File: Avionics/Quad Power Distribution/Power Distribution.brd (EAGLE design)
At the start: 50 x 50 mm, 55 parts, among them U1 LMP8645, U10 SERVOPLUGTHROUGHHOLE_0.1PITCH, U2 LMP8645, U3 LMP8645, U4 LMP8645, U5 LMP8645, U6 ADP2302, U7 SERVOPLUGTHROUGHHOLE_0.1PITCH, U8 SERVOPLUGTHROUGHHOLE_0.1PITCH, U9 SERVOPLUGTHROUGHHOLE_0.1PITCH

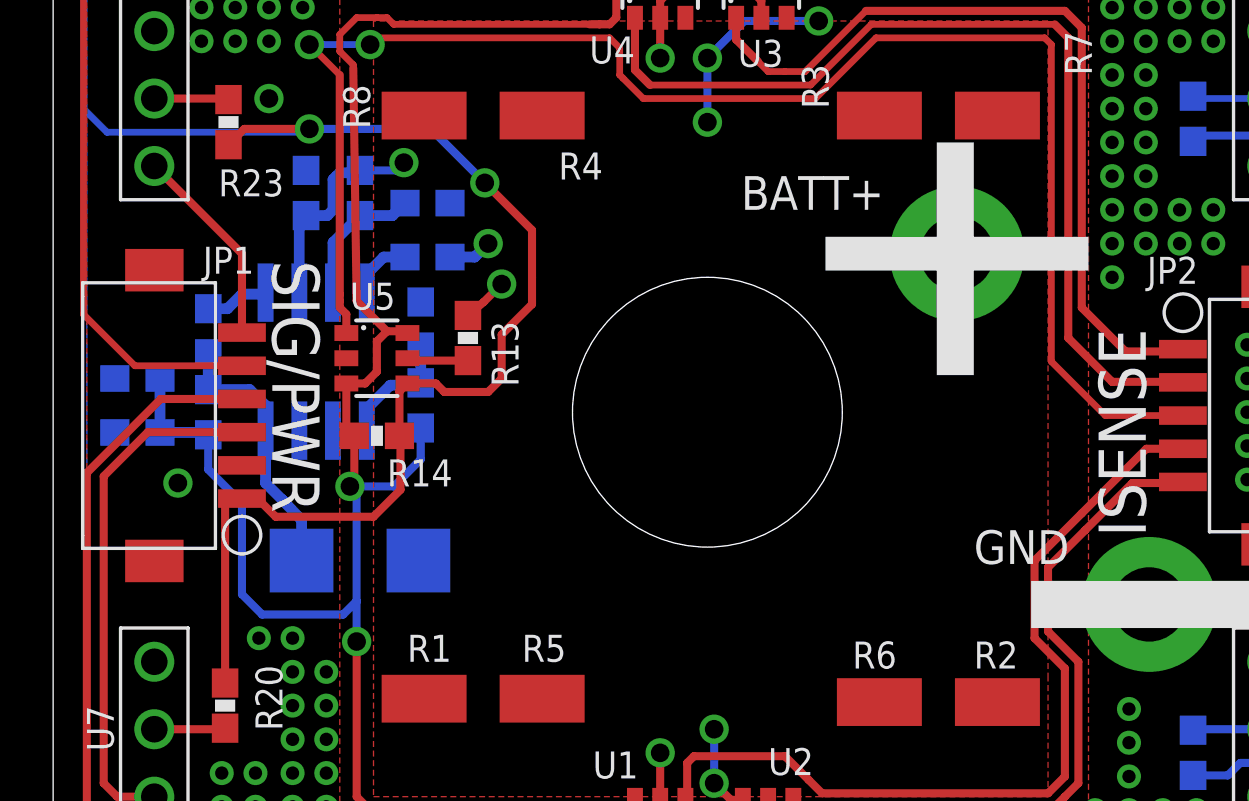
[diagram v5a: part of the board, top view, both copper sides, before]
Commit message: Committed file outputs and cleaned silk. Added shock hazard symbol
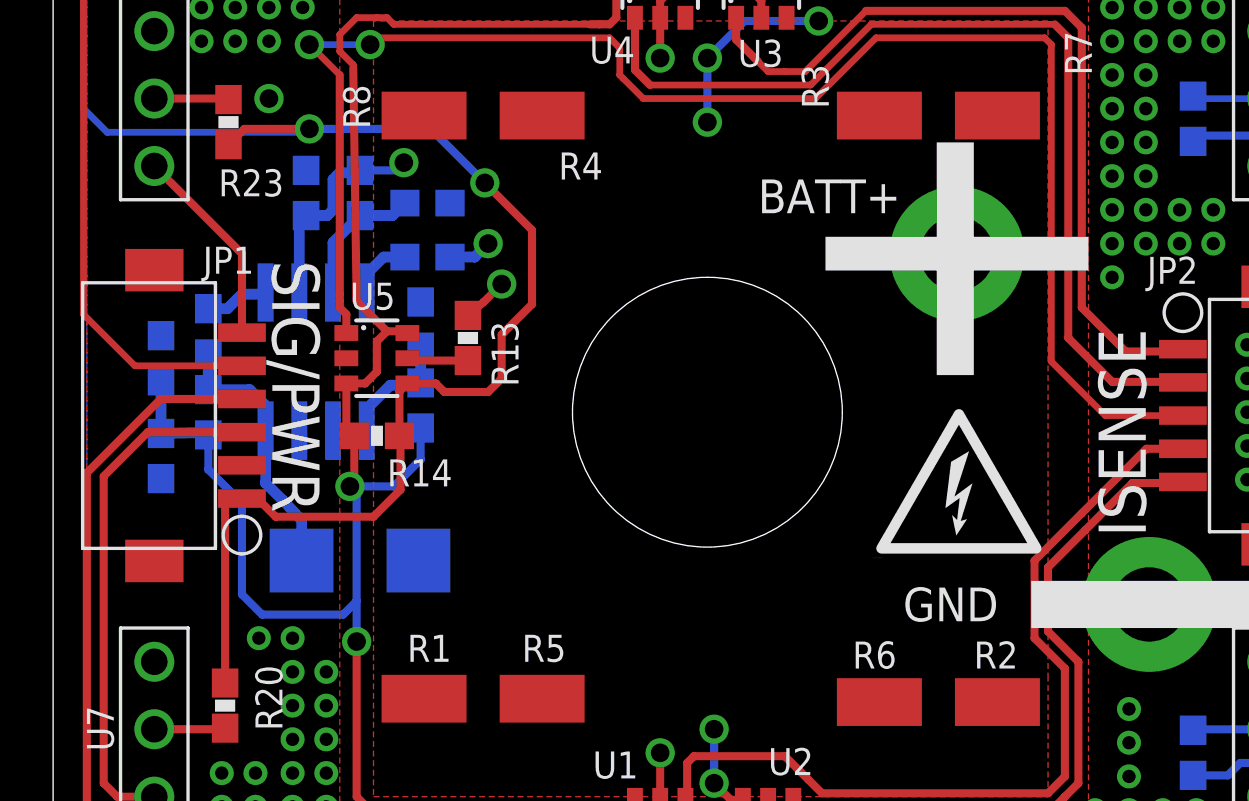
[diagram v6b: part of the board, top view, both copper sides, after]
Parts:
- added U$5: (no value), Shared Libraries:SHOCK_HAZARD
- moved C2 1.26 mm to (4.06, 23.0), turned to 270 degrees
- moved C3 1.17 mm to (4.06, 26.7), turned to 90 degrees
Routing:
- net GND: vias 150 -> 149
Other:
- board text added: "+"
- board text added: "-"
- board text added: "I1"
- board text added: "I2"
- board text added: "I3"
- board text added: "I4"
- board text added: "I5"
- board text added: "S1"
- board text added: "S2"
- board text added: "S3"
- board text added: "S4"
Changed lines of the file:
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@@
 <layer number="21" name="tPlace" color="7" fill="1" visible="yes" active="yes"/>
 <layer number="22" name="bPlace" color="7" fill="1" visible="yes" active="yes"/>
-<layer number="23" name="tOrigins" color="15" fill="1" visible="no" active="yes"/>
-<layer number="24" name="bOrigins" color="15" fill="1" visible="no" active="yes"/>
+<layer number="23" name="tOrigins" color="15" fill="1" visible="yes" active="yes"/>
+<layer number="24" name="bOrigins" color="15" fill="1" visible="yes" active="yes"/>
 <layer number="25" name="tNames" color="7" fill="1" visible="yes" active="yes"/>
 <layer number="26" name="bNames" color="7" fill="1" visible="yes" active="yes"/>
@@
 <text x="8.255" y="30.353" size="1.778" layer="21" rot="SR270">SIG/PWR</text>
 <text x="41.148" y="19.939" size="1.778" layer="21" rot="SR90">ISENSE</text>
+<text x="1.524" y="20.066" size="1.27" layer="22" rot="MR90">+</text>
+<text x="2.413" y="21.59" size="1.27" layer="22" rot="SMR0">-</text>
+<text x="3.175" y="22.733" size="1.27" layer="22" rot="SMR0">S1</text>
+<text x="3.175" y="24.384" size="1.27" layer="22" rot="SMR0">S2</text>
+<text x="3.175" y="26.035" size="1.27" layer="22" rot="SMR0">S3</text>
+<text x="3.175" y="27.686" size="1.27" layer="22" rot="SMR0">S4</text>
+<text x="48.514" y="22.225" size="1.27" layer="22" rot="MR0">I1</text>
+<text x="48.514" y="20.574" size="1.27" layer="22" rot="MR0">I2</text>
+<text x="48.514" y="23.876" size="1.27" layer="22" rot="MR0">I5</text>
+<text x="48.514" y="25.654" size="1.27" layer="22" rot="MR0">I4</text>
+<text x="48.514" y="27.305" size="1.27" layer="22" rot="MR0">I3</text>
 </plain>
 <attributes>
@@
 <element name="U$4" library="SparkFun-Electromechanical" package="STAND-OFF" value="" x="3.81" y="45.466"/>
 <element name="BATT+" library="Shared Libraries" package="10AWG_SOLDERPAD" value="10AWG_PAD" x="34.036" y="30.607" smashed="yes">
-<attribute name="NAME" x="25.908" y="32.258" size="1.27" layer="21"/>
+<attribute name="NAME" x="26.543" y="32.131" size="1.27" layer="21"/>
 </element>
 <element name="GND" library="Shared Libraries" package="10AWG_SOLDERPAD" value="10AWG_PAD" x="41.275" y="17.399" smashed="yes">
-<attribute name="NAME" x="34.671" y="18.923" size="1.27" layer="21"/>
+<attribute name="NAME" x="32.004" y="16.764" size="1.27" layer="21"/>
 </element>
 <element name="U6" library="Shared Libraries" package="SOIC8" value="ADP2302" x="9.906" y="26.543" smashed="yes" rot="MR180">
@@
 </element>
 <element name="R17" library="Shared Libraries" package="0603-RES" value="10.2k" x="14.097" y="32.512" smashed="yes" rot="MR180">
-<attribute name="NAME" x="15.621" y="32.639" size="1.016" layer="26" font="vector" rot="MR180"/>
+<attribute name="NAME" x="13.716" y="34.925" size="1.016" layer="26" font="vector" rot="MR180"/>
 <attribute name="VALUE" x="13.081" y="33.655" size="0.4064" layer="28" font="vector" rot="MR180" display="off"/>
 </element>
@@
 </element>
 <element name="C1" library="SparkFun-Capacitors" package="0603-CAP" value="10uF" x="9.525" y="32.893" smashed="yes" rot="MR90">
-<attribute name="NAME" x="7.366" y="32.893" size="1.016" layer="26" font="vector" rot="MR90"/>
+<attribute name="NAME" x="7.874" y="33.401" size="1.016" layer="26" font="vector" rot="MR90"/>
 <attribute name="VALUE" x="8.382" y="31.877" size="0.4064" layer="28" font="vector" rot="MR90" display="off"/>
 </element>
-<element name="C2" library="SparkFun-Capacitors" package="0603-CAP" value="22uF" x="3.175" y="23.876" smashed="yes" rot="MR0">
-<attribute name="NAME" x="3.175" y="21.844" size="1.016" layer="26" font="vector" rot="MR0"/>
-<attribute name="VALUE" x="4.191" y="22.733" size="0.4064" layer="28" font="vector" rot="MR0" display="off"/>
-</element>
-<element name="C3" library="SparkFun-Capacitors" package="0603-CAP" value="22uF" x="3.175" y="25.908" smashed="yes" rot="MR0">
-<attribute name="NAME" x="3.175" y="27.051" size="1.016" layer="26" font="vector" rot="MR0"/>
-<attribute name="VALUE" x="4.191" y="24.765" size="0.4064" layer="28" font="vector" rot="MR0" display="off"/>
+<element name="C2" library="SparkFun-Capacitors" package="0603-CAP" value="22uF" x="4.064" y="22.987" smashed="yes" rot="MR270">
+<attribute name="NAME" x="4.572" y="21.336" size="1.016" layer="26" font="vector" rot="MR270"/>
+<attribute name="VALUE" x="5.207" y="24.003" size="0.4064" layer="28" font="vector" rot="MR270" display="off"/>
+</element>
+<element name="C3" library="SparkFun-Capacitors" package="0603-CAP" value="22uF" x="4.064" y="26.67" smashed="yes" rot="MR90">
+<attribute name="NAME" x="3.683" y="28.321" size="1.016" layer="26" font="vector" rot="MR90"/>
+<attribute name="VALUE" x="2.921" y="25.654" size="0.4064" layer="28" font="vector" rot="MR90" display="off"/>
 </element>
 <element name="C4" library="SparkFun-Capacitors" package="0603-CAP" value="0.1uF" x="5.842" y="27.686" smashed="yes" rot="MR270">
-<attribute name="NAME" x="5.08" y="29.21" size="1.016" layer="26" font="vector" rot="MR270"/>
+<attribute name="NAME" x="5.969" y="31.242" size="1.016" layer="26" font="vector" rot="MR270"/>
 <attribute name="VALUE" x="6.985" y="28.702" size="0.4064" layer="28" font="vector" rot="MR270" display="off"/>
 </element>
@@
 </element>
 <element name="D1" library="diode" package="SMB" value="SSB43L" x="11.557" y="19.05" smashed="yes" rot="MR180">
-<attribute name="NAME" x="12.446" y="16.764" size="1.016" layer="26" rot="MR180"/>
+<attribute name="NAME" x="17.272" y="18.542" size="1.016" layer="26" rot="MR0"/>
 <attribute name="VALUE" x="9.398" y="22.479" size="1.27" layer="28" rot="MR180" display="off"/>
 </element>
@@
 <attribute name="NAME" x="41.193" y="29.472" size="1.016" layer="21"/>
 </element>
+<element name="U$5" library="Shared Libraries" package="SHOCK_HAZARD" value="" x="30.861" y="19.177"/>
 </elements>
 <signals>
@@
 <via x="35.814" y="47.625" extent="1-16" drill="0.5"/>
 <contactref element="JP1" pad="P2"/>
-<via x="4.699" y="21.971" extent="1-16" drill="0.7" shape="square"/>
+<wire x1="6.35" y1="18.796" x2="6.35" y2="18.796" width="0" layer="19" extent="1-16"/>
 <via x="7.62" y="11.049" extent="1-16" drill="0.5"/>
 <via x="41.783" y="8.382" extent="1-16" drill="0.5"/>
@@
 <contactref element="R18" pad="2"/>
 <contactref element="L1" pad="2"/>
-<wire x1="4.025" y1="23.876" x2="5.754" y2="23.876" width="0.4064" layer="16"/>
+<wire x1="4.064" y1="23.837" x2="5.754" y2="23.876" width="0.4064" layer="16"/>
 <wire x1="5.754" y1="23.876" x2="5.842" y2="23.788" width="0.4064" layer="16"/>
-<wire x1="4.025" y1="23.876" x2="4.025" y2="25.908" width="0.4064" layer="16"/>
+<wire x1="4.064" y1="23.837" x2="4.064" y2="25.82" width="0.4064" layer="16"/>
 <contactref element="U2" pad="6"/>
 <contactref element="U1" pad="6"/>
